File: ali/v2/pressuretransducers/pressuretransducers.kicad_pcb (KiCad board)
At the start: 4 copper layers, 85 x 76 mm, 237 parts, among them J1 Conn_02x01, J10 Conn_01x02, J11 Conn_01x02, J12 Conn_01x02, J13 Conn_01x02, J14 Conn_01x02, J15 Conn_01x02, J16 Conn_01x02, J17 Conn_01x02, J18 Conn_01x02, J19 Conn_01x02, J2 Conn_01x05, J20 Conn_01x02, J21 Conn_01x02, J22 Conn_01x02, J23 Conn_01x02, J24 Conn_01x02, J25 Conn_01x02, J3 USB_C_Receptacle_USB2.0_16P, J4 Conn_02x09_Counter_Clockwise, J5 Conn_01x15, J6 Screw_Terminal_01x02, J7 Screw_Terminal_01x02, J8 Conn_01x03, J9 Vertical Ethernet, SW1 SKRPANE010, U1 STM32H563RIV6, U2 AP2112K-3.3, U3 TJA1462ATK, U4 LAN8742AI, U5 ADS131M08IRSN, U6 ADS131M08IRSN, Y1 25 MHz, Y2 8.192 MHz, Y3 25 MHz

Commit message: The other half of the great 10.0.6 migration
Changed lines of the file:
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@@
 			)
 		)
-		(property "Description" "8-Channel, Simultaneously-Sampling, 24-Bit, Delta-Sigma ADC"
+		(property "Description" "8-channel, 24-bit, simultaneous-sampling delta-sigma ADC, 32 kSPS, PGA 1-128, SPI, WQFN-32 with thermal pad (Texas RSN)"
 			(at 0 0 0)
 			(layer "F.Fab")
@@
 			)
 		)
-		(property "Description" "8-Channel, Simultaneously-Sampling, 24-Bit, Delta-Sigma ADC"
+		(property "Description" "8-channel, 24-bit, simultaneous-sampling delta-sigma ADC, 32 kSPS, PGA 1-128, SPI, WQFN-32 with thermal pad (Texas RSN)"
 			(at 0 0 0)
 			(layer "F.Fab")
@@
 	)
 	(gr_text "+24V"
-		(at 134.9125 81.425 180)
+		(at 136.1375 80.6 180)
 		(layer "F.SilkS")
 		(effects
@@
 			(polygon
 				(pts
-					(xy 139.403025 78.885153) (xy 138.882055 78.885153) (xy 138.882055 79.691154) (xy 138.090525 79.691154)
-					(xy 138.090525 80.18538) (xy 138.882055 80.18538) (xy 138.882055 80.991198) (xy 139.403025 80.991198)
-					(xy 139.403025 80.18538) (xy 140.19254 80.18538) (xy 140.19254 79.691154) (xy 139.403025 79.691154)
+					(xy 140.628025 78.060153) (xy 140.107055 78.060153) (xy 140.107055 78.866154) (xy 139.315525 78.866154)
+					(xy 139.315525 79.36038) (xy 140.107055 79.36038) (xy 140.107055 80.166198) (xy 140.628025 80.166198)
+					(xy 140.628025 79.36038) (xy 141.41754 79.36038) (xy 141.41754 78.866154) (xy 140.628025 78.866154)
 				)
 			)
 			(polygon
 				(pts
-					(xy 137.55545 78.425) (xy 135.393901 78.425) (xy 135.393901 78.939741) (xy 136.685885 78.939741)
-					(xy 136.685885 78.962273) (xy 136.224632 79.417114) (xy 135.985266 79.645606) (xy 135.79659 79.844729)
-					(xy 135.679725 79.985631) (xy 135.588937 80.114899) (xy 135.528865 80.220885) (xy 135.485132 80.322277)
-					(xy 135.457078 80.416568) (xy 135.440864 80.510265) (xy 135.434934 80.617873) (xy 135.44073 80.722555)
-					(xy 135.457855 80.822605) (xy 135.485822 80.917365) (xy 135.524271 81.006725) (xy 135.631612 81.168321)
-					(xy 135.778366 81.304688) (xy 135.963422 81.41194) (xy 136.185232 81.485083) (xy 136.309547 81.507176)
-					(xy 136.441189 81.518537) (xy 136.511679 81.520045) (xy 136.644283 81.514246) (xy 136.770404 81.4971)
-					(xy 136.887871 81.469457) (xy 136.998009 81.431515) (xy 137.098555 81.384571) (xy 137.191054 81.328381)
-					(xy 137.273552 81.26457) (xy 137.347375 81.192504) (xy 137.411146 81.113792) (xy 137.465626 81.027699)
-					(xy 137.510024 80.935396) (xy 137.544443 80.836446) (xy 137.568438 80.731272) (xy 137.581628 80.620065)
-					(xy 137.58421 80.542035) (xy 136.985388 80.542035) (xy 136.979618 80.629955) (xy 136.962674 80.71005)
-					(xy 136.936154 80.779726) (xy 136.900182 80.841304) (xy 136.856229 80.893441) (xy 136.804145 80.93708)
-					(xy 136.677005 80.997575) (xy 136.518576 81.019585) (xy 136.515709 81.019591) (xy 136.430124 81.013809)
-					(xy 136.350522 80.99678) (xy 136.279503 80.969758) (xy 136.216021 80.932913) (xy 136.162627 80.888334)
-					(xy 136.117954 80.835378) (xy 136.083646 80.776213) (xy 136.059119 80.709872) (xy 136.042 80.579038)
-					(xy 136.047817 80.498443) (xy 136.065093 80.422004) (xy 136.133882 80.274174) (xy 136.264821 80.103842)
-					(xy 136.472661 79.890457) (xy 137.55545 78.875994)
+					(xy 138.78045 77.6) (xy 136.618901 77.6) (xy 136.618901 78.114741) (xy 137.910885 78.114741) (xy 137.910885 78.137273)
+					(xy 137.449632 78.592114) (xy 137.210266 78.820606) (xy 137.02159 79.019729) (xy 136.904725 79.160631)
+					(xy 136.813937 79.289899) (xy 136.753865 79.395885) (xy 136.710132 79.497277) (xy 136.682078 79.591568)
+					(xy 136.665864 79.685265) (xy 136.659934 79.792873) (xy 136.66573 79.897555) (xy 136.682855 79.997605)
+					(xy 136.710822 80.092365) (xy 136.749271 80.181725) (xy 136.856612 80.343321) (xy 137.003366 80.479688)
+					(xy 137.188422 80.58694) (xy 137.410232 80.660083) (xy 137.534547 80.682176) (xy 137.666189 80.693537)
+					(xy 137.736679 80.695045) (xy 137.869283 80.689246) (xy 137.995404 80.6721) (xy 138.112871 80.644457)
+					(xy 138.223009 80.606515) (xy 138.323555 80.559571) (xy 138.416054 80.503381) (xy 138.498552 80.43957)
+					(xy 138.572375 80.367504) (xy 138.636146 80.288792) (xy 138.690626 80.202699) (xy 138.735024 80.110396)
+					(xy 138.769443 80.011446) (xy 138.793438 79.906272) (xy 138.806628 79.795065) (xy 138.80921 79.717035)
+					(xy 138.210388 79.717035) (xy 138.204618 79.804955) (xy 138.187674 79.88505) (xy 138.161154 79.954726)
+					(xy 138.125182 80.016304) (xy 138.081229 80.068441) (xy 138.029145 80.11208) (xy 137.902005 80.172575)
+					(xy 137.743576 80.194585) (xy 137.740709 80.194591) (xy 137.655124 80.188809) (xy 137.575522 80.17178)
+					(xy 137.504503 80.144758) (xy 137.441021 80.107913) (xy 137.387627 80.063334) (xy 137.342954 80.010378)
+					(xy 137.308646 79.951213) (xy 137.284119 79.884872) (xy 137.267 79.754038) (xy 137.272817 79.673443)
+					(xy 137.290093 79.597004) (xy 137.358882 79.449174) (xy 137.489821 79.278842) (xy 137.697661 79.065457)
+					(xy 138.78045 78.050994)
 				)
 			)
 			(polygon
 				(pts
-					(xy 133.561347 78.964288) (xy 135.023507 78.964288) (xy 135.023507 79.458513) (xy 133.745812 81.484874)
-					(xy 132.960327 81.484874) (xy 132.960327 80.795743) (xy 133.548891 80.795743) (xy 133.57362 80.795743)
-					(xy 134.391895 79.493318) (xy 134.391895 79.468771) (xy 133.548891 79.468771) (xy 133.548891 80.795743)
-					(xy 132.960327 80.795743) (xy 132.960327 79.468771) (xy 132.578941 79.468771) (xy 132.578941 78.964288)
-					(xy 132.960327 78.964288) (xy 132.960327 78.425) (xy 133.561347 78.425)
+					(xy 134.786347 78.139288) (xy 136.248507 78.139288) (xy 136.248507 78.633513) (xy 134.970812 80.659874)
+					(xy 134.185327 80.659874) (xy 134.185327 79.970743) (xy 134.773891 79.970743) (xy 134.79862 79.970743)
+					(xy 135.616895 78.668318) (xy 135.616895 78.643771) (xy 134.773891 78.643771) (xy 134.773891 79.970743)
+					(xy 134.185327 79.970743) (xy 134.185327 78.643771) (xy 133.803941 78.643771) (xy 133.803941 78.139288)
+					(xy 134.185327 78.139288) (xy 134.185327 77.6) (xy 134.786347 77.6)
 				)
 			)
 			(polygon
 				(pts
-					(xy 131.219547 78.425) (xy 130.401272 78.425) (xy 129.355302 81.484874) (xy 130.046448 81.484874)
-					(xy 130.518142 80.008243) (xy 130.759584 79.122049) (xy 130.807387 78.930033) (xy 130.960138 79.50843)
-					(xy 131.106707 80.008243) (xy 131.594887 81.484874) (xy 132.290063 81.484874)
+					(xy 132.444547 77.6) (xy 131.626272 77.6) (xy 130.580302 80.659874) (xy 131.271448 80.659874) (xy 131.743142 79.183243)
+					(xy 131.984584 78.297049) (xy 132.032387 78.105033) (xy 132.185138 78.68343) (xy 132.331707 79.183243)
+					(xy 132.819887 80.659874) (xy 133.515063 80.659874)
 				)
 			)
@@
 	)
 	(gr_text "+"
-		(at 134.6125 73.625 0)
+		(at 129.3075 72.625 0)
 		(layer "F.SilkS" knockout)
 		(effects
@@
 			(polygon
 				(pts
-					(xy 136.165396 77.402006) (xy 136.860022 77.402006) (xy 136.860022 76.327337) (xy 137.915396 76.327337)
-					(xy 137.915396 75.671057) (xy 136.860022 75.671057) (xy 136.860022 74.596632) (xy 136.165396 74.596632)
-					(xy 136.165396 75.671057) (xy 135.112709 75.671057) (xy 135.112709 76.327337) (xy 136.165396 76.327337)
+					(xy 130.860396 76.402006) (xy 131.555022 76.402006) (xy 131.555022 75.327337) (xy 132.610396 75.327337)
+					(xy 132.610396 74.671057) (xy 131.555022 74.671057) (xy 131.555022 73.596632) (xy 130.860396 73.596632)
+					(xy 130.860396 74.671057) (xy 129.807709 74.671057) (xy 129.807709 75.327337) (xy 130.860396 75.327337)
 				)
 			)
@@
 	)
 	(gr_text "-"
-		(at 129.8925 73.525 0)
+		(at 124.5875 72.525 0)
 		(layer "F.SilkS")
 		(effects
@@
 			(polygon
 				(pts
-					(xy 132.688164 75.524162) (xy 130.37091 75.524162) (xy 130.37091 76.180443) (xy 132.688164 76.180443)
+					(xy 127.383164 74.524162) (xy 125.06591 74.524162) (xy 125.06591 75.180443) (xy 127.383164 75.180443)
 				)
 			)

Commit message: Fix 50R/60R widths
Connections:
- net Net-(J8-Pin_1) renamed /Connectivity/CAN+
- net Net-(J8-Pin_2) renamed /Connectivity/CAN-
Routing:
- net GND: track 2.94 -> 5.64 mm, vias 475 -> 481
- net /Connectivity/RX+: track 14.8 -> 14.1 mm

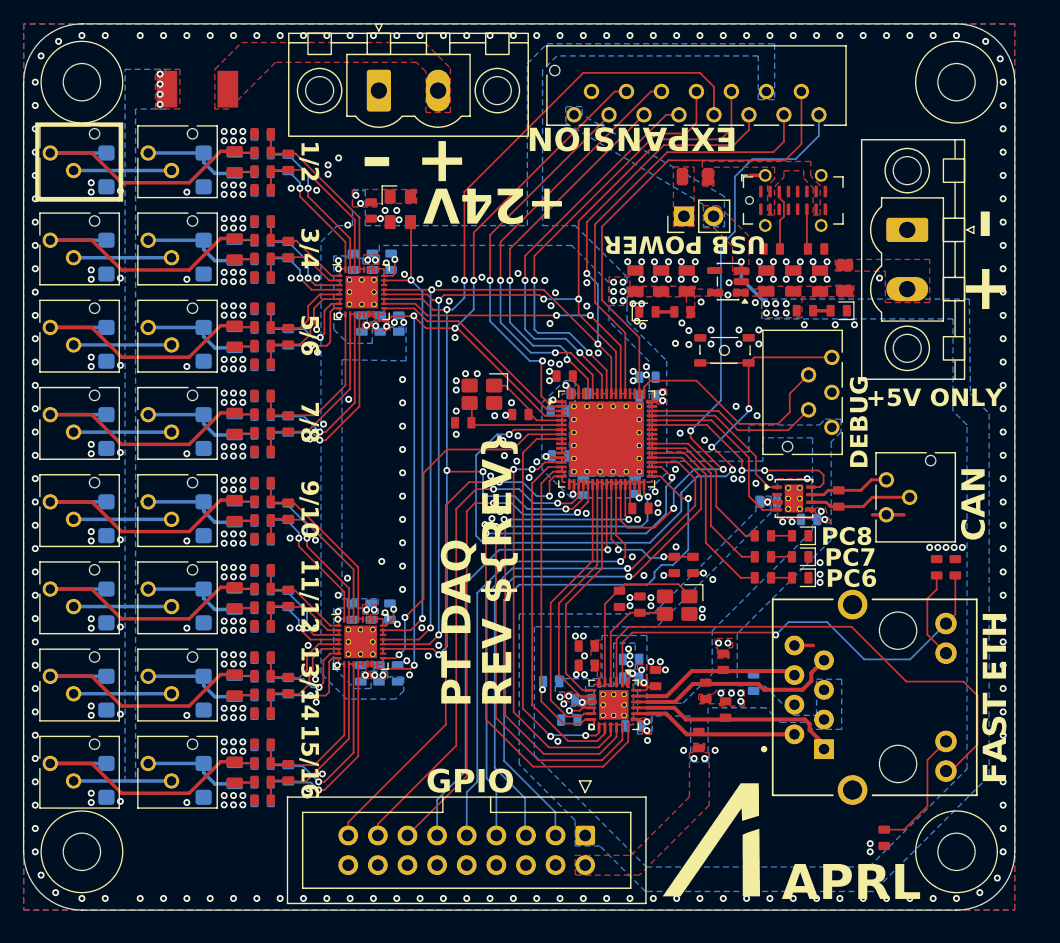
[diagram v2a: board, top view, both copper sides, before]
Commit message: Document setup, update template, and use an ampersand when referring to APRL
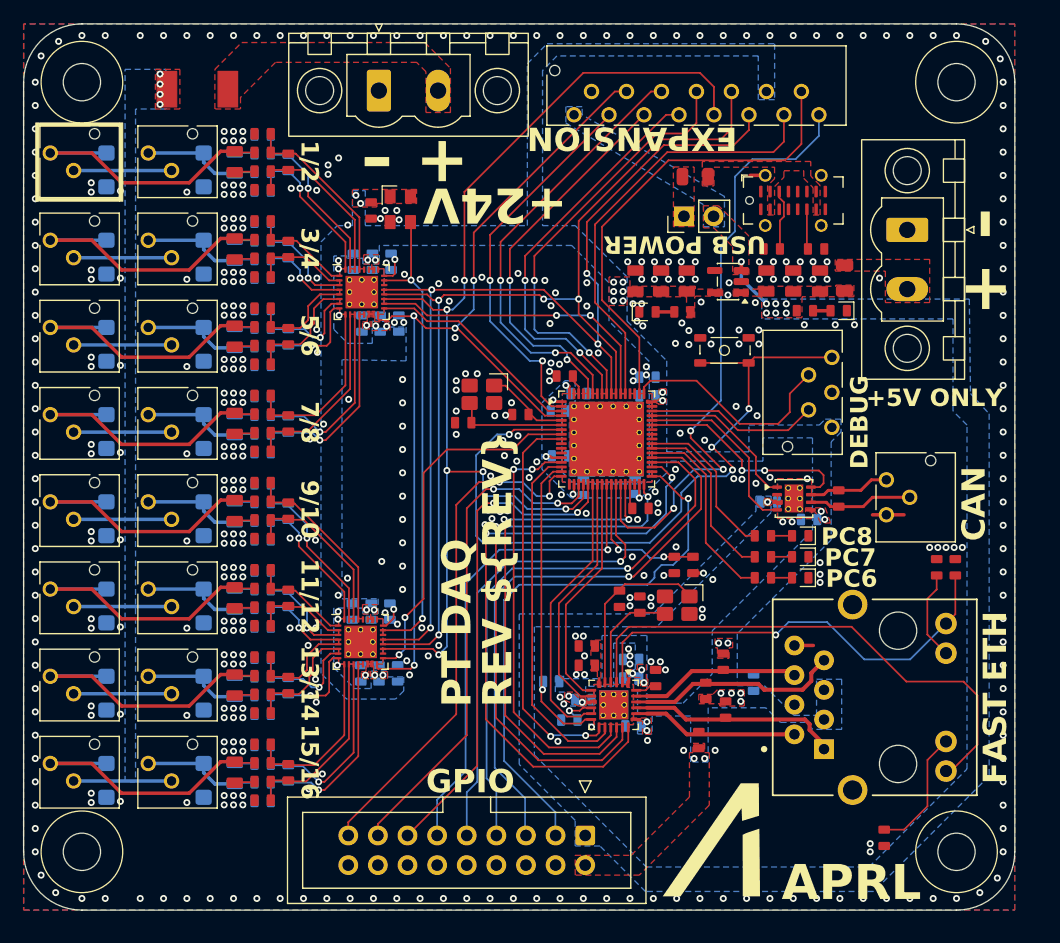
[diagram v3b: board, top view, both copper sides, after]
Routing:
- net Net-(D13-K): track 10.2 -> 9.66 mm
- net Net-(D7-K): track 10.2 -> 9.66 mm
- net Net-(D21-K): track 10.2 -> 9.66 mm
- net Net-(D19-K): track 10.2 -> 9.66 mm
- net Net-(D17-K): track 10.2 -> 9.66 mm
- net Net-(D15-K): track 10.2 -> 9.66 mm
